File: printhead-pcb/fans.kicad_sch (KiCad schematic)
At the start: 18 parts, among them J4 FAN0, J5 FAN2, J6 FAN1, J7 FAN3, Q1 DTC143E, Q2 DTC143E, Q3 DTC143E, Q4 DTC143E, U2 EMC2302-2-AIZL-TR, U3 EMC2302-2-AIZL-TR

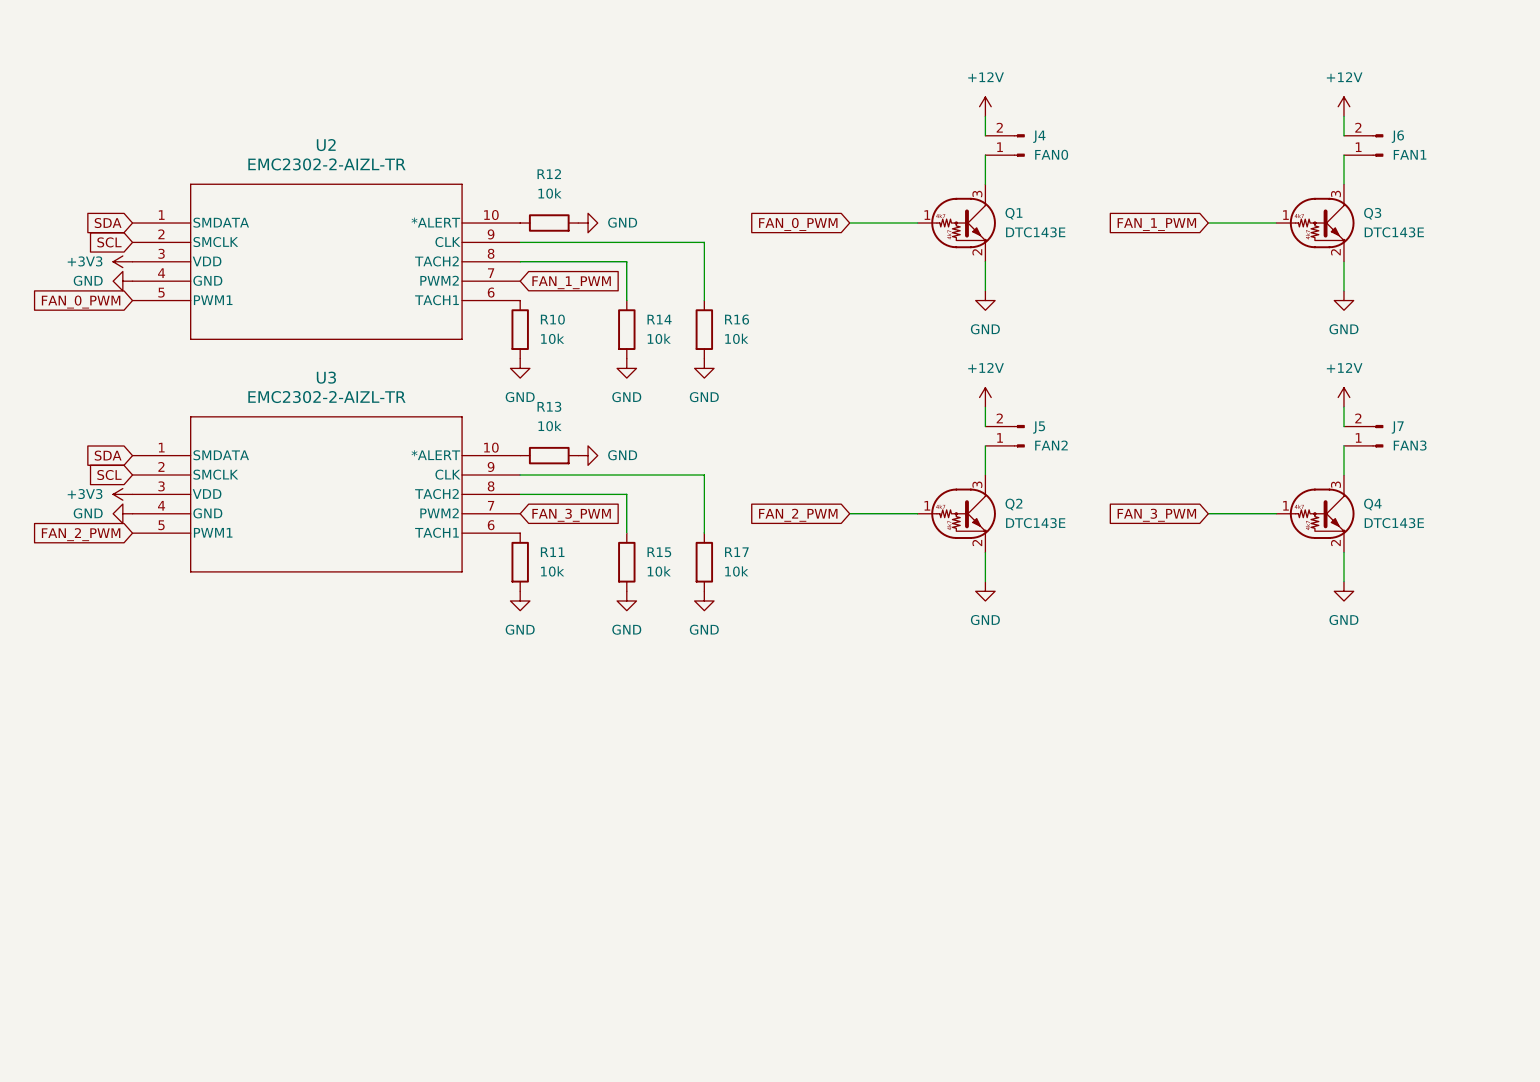
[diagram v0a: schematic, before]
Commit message: removed fan controller and added 2 fans for on off functionality.
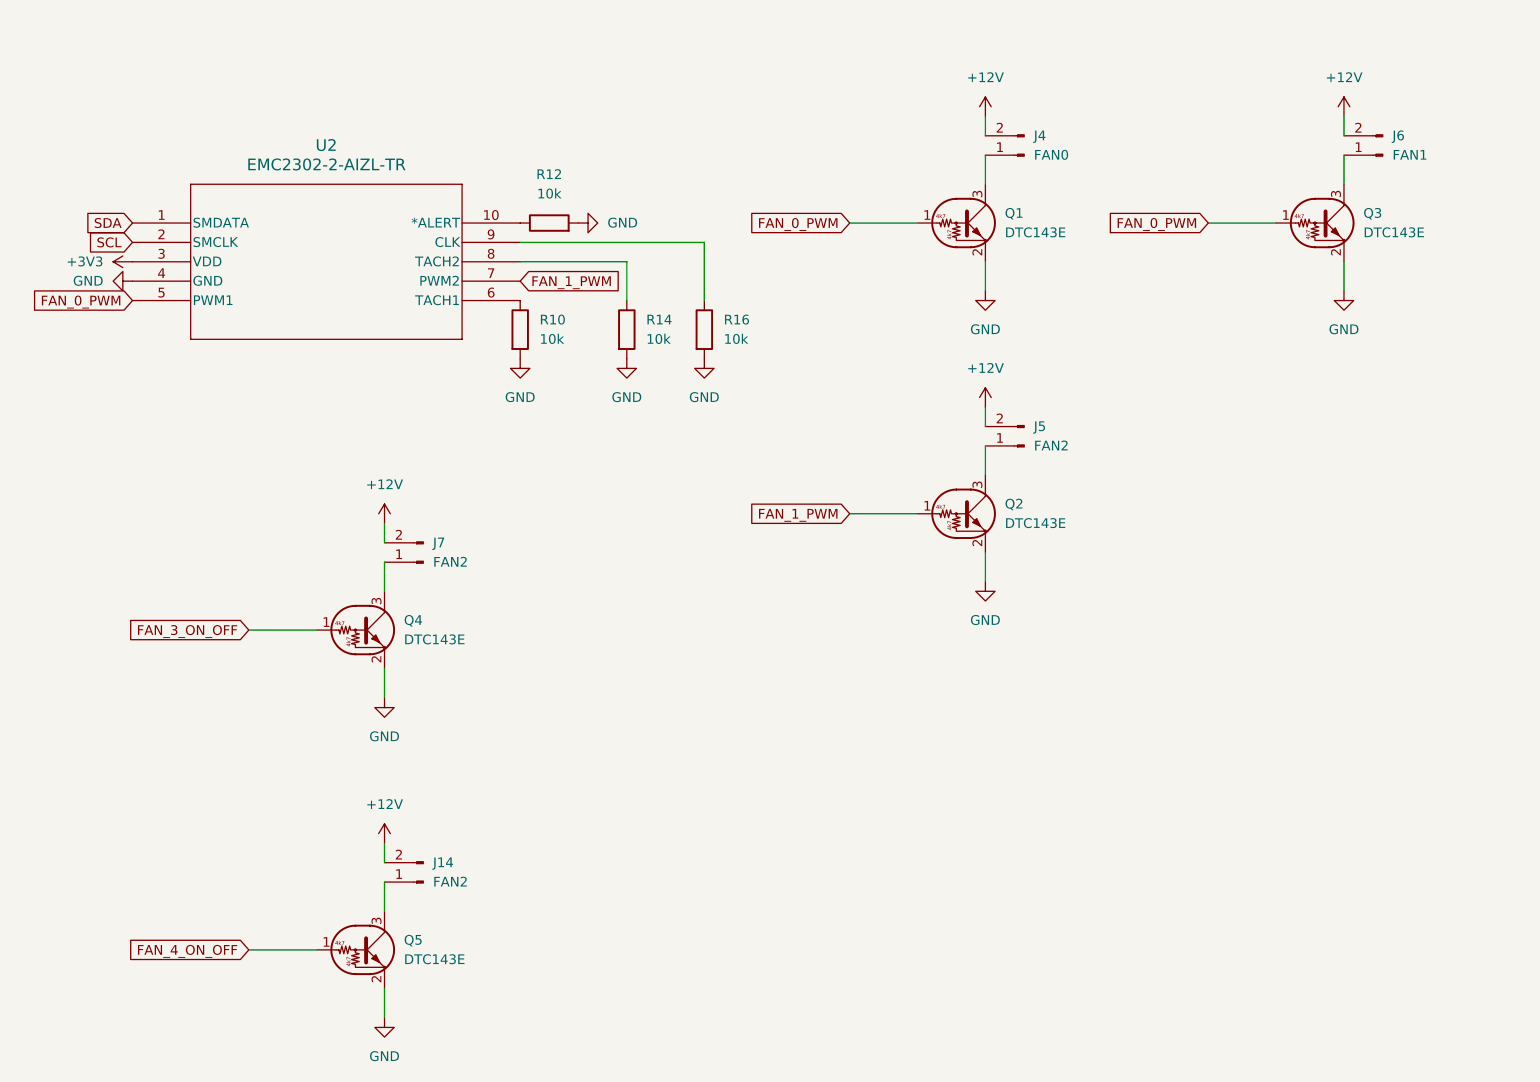
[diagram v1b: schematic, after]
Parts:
- removed R11, R13, R15, R17: 10k, Resistor_SMD:R_0402_1005Metric, symbol Device:R
- removed U3: EMC2302-2-AIZL-TR, EMC2302-2-AIZL-TR:MSOP10_MC_MCH, symbol EMC2302-2-AIZL-TR:EMC2302-2-AIZL-TR
- added J14: FAN2, Connector_JST:JST_EH_B2B-EH-A_1x02_P2.50mm_Vertical, symbol Connector:Conn_01x02_Male
- added Q5: DTC143E, Package_TO_SOT_SMD:SOT-723, symbol Transistor_BJT:DTC143E
- J7: value FAN3 -> FAN2
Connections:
- net FAN_2_PWM is gone; now on net FAN_1_PWM: Q2.1 (B)
- net +12V: now also J14.2 (Pin_2)
- net FAN_0_PWM: now also Q3.1 (B)
- net FAN_1_PWM: no longer Q3.1 (B)
- net GND: now also Q5.2 (E)
- net FAN_3_PWM renamed FAN_3_ON_OFF
- new net: J14.1 (Pin_1), Q5.3 (C)
- new net FAN_4_ON_OFF: Q5.1 (B)

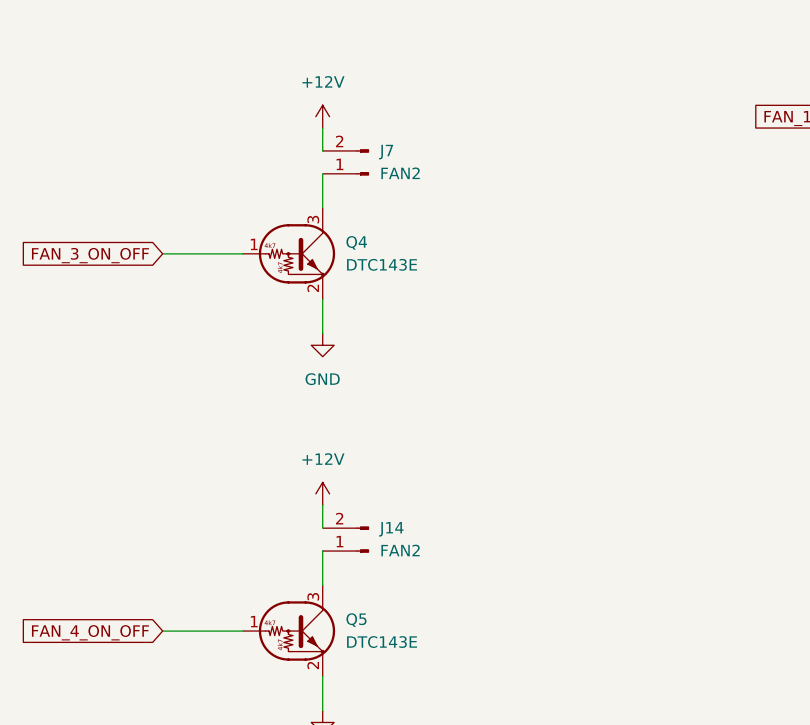
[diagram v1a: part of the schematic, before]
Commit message: changed fan labels
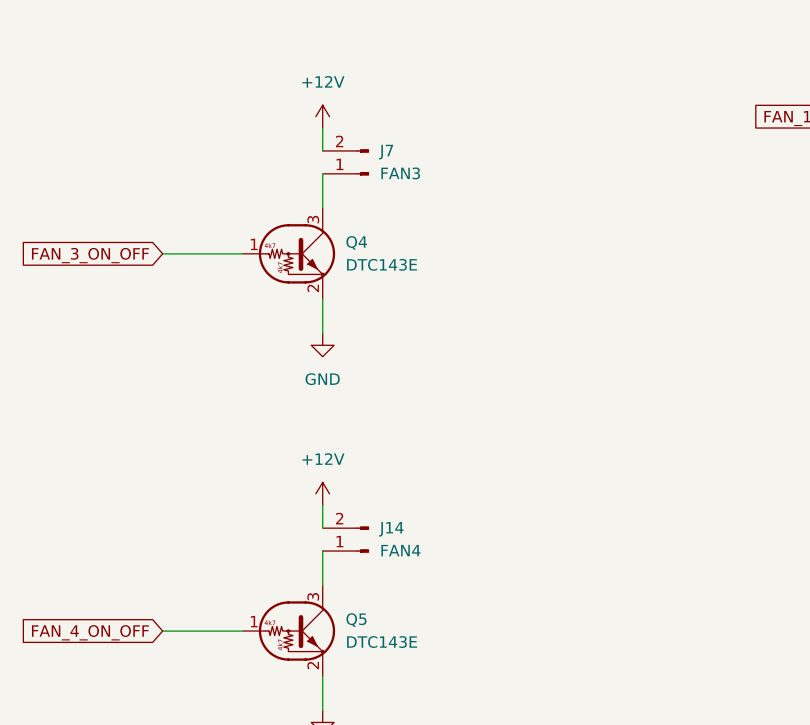
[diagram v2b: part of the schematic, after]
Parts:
- J14: value FAN2 -> FAN4
- J7: value FAN2 -> FAN3
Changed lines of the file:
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@@
 			)
 		)
-		(property "Value" "FAN2"
+		(property "Value" "FAN3"
 			(at 107.95 121.9199 0)
 			(effects
@@
 			)
 		)
-		(property "Value" "FAN2"
+		(property "Value" "FAN4"
 			(at 107.95 163.8299 0)
 			(effects

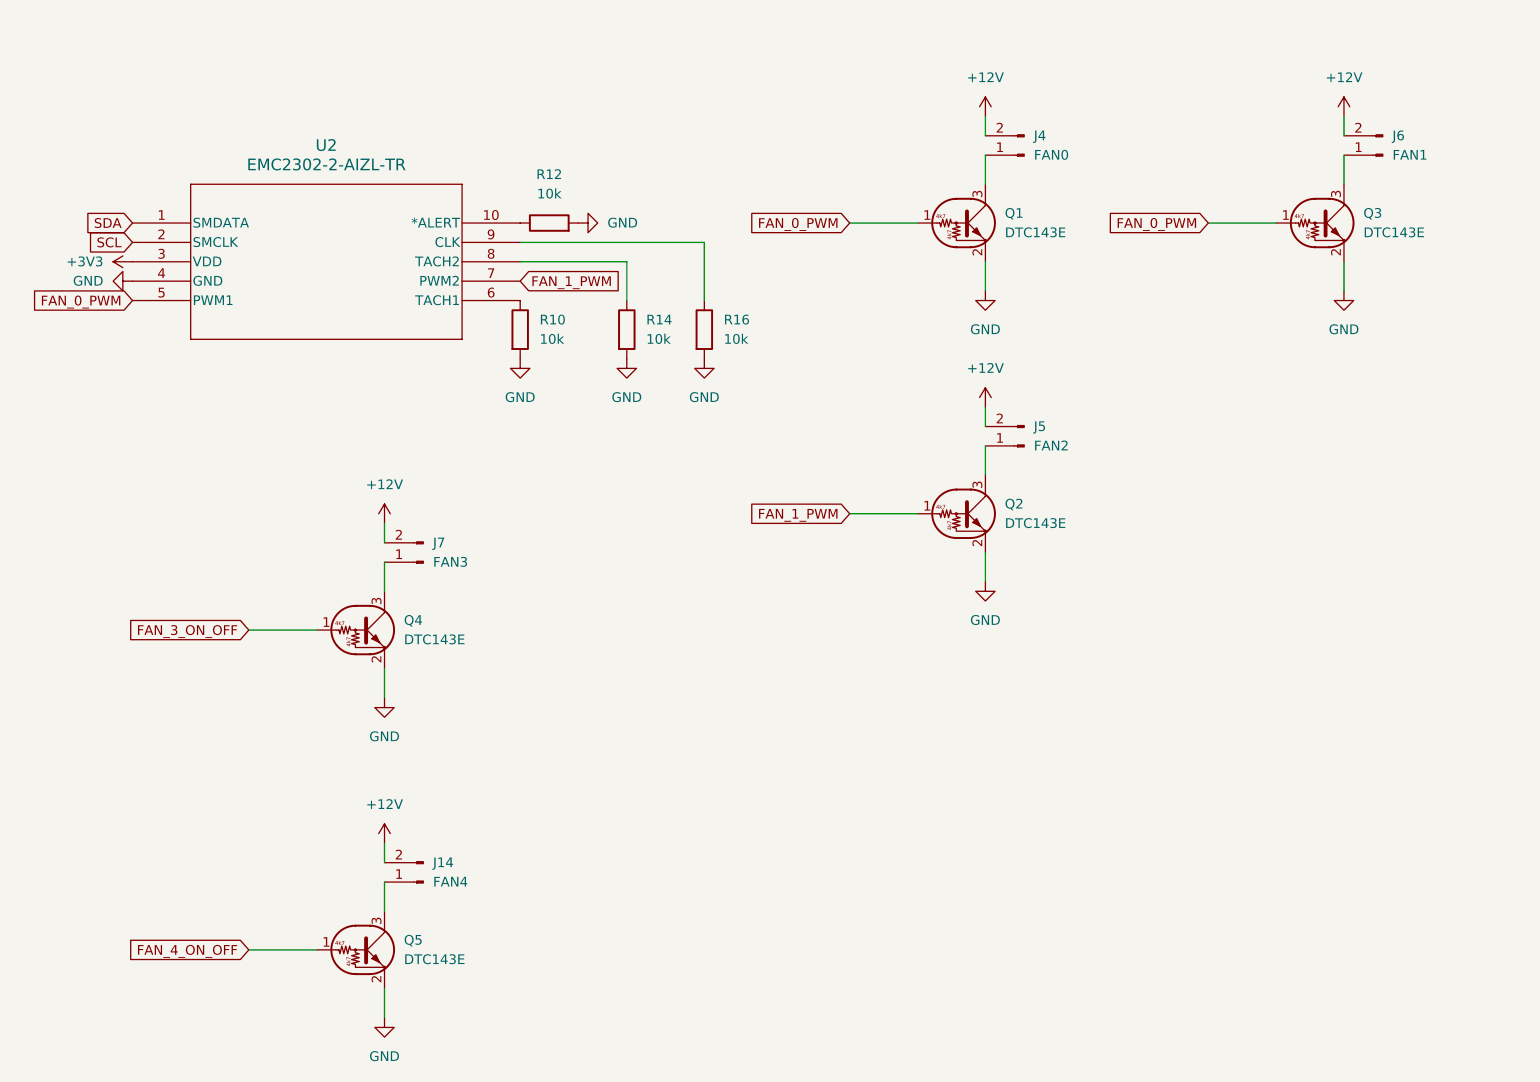
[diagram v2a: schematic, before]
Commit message: removed led driver, added RJ45 (data connector), fan 3. 4. on off
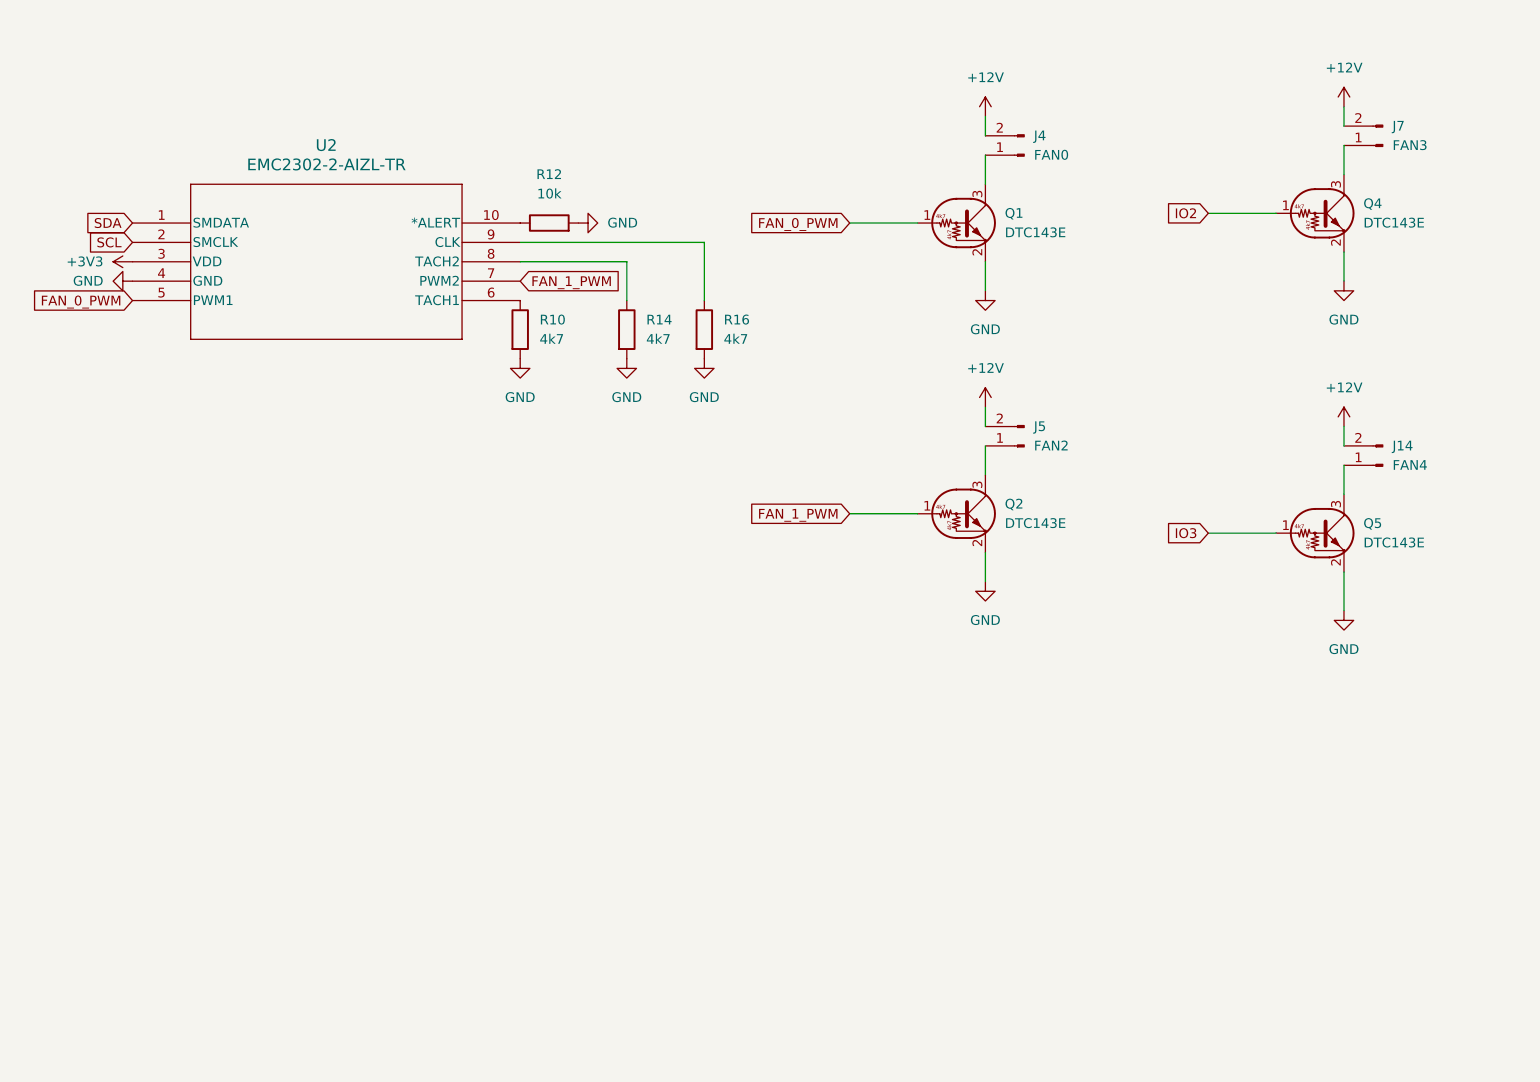
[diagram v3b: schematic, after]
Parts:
- removed J6: FAN1, Connector_JST:JST_EH_S2B-EH_1x02_P2.50mm_Horizontal, symbol Connector:Conn_01x02_Male
- removed Q3: DTC143E, Package_TO_SOT_SMD:SOT-723, symbol Transistor_BJT:DTC143E
- R10, R14, R16: value 10k -> 4k7
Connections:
- net FAN_3_ON_OFF renamed IO2
- net FAN_4_ON_OFF renamed IO3
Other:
- moved on the sheet: J14, J7, Q4, Q5

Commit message: Beschriftungen im Schaltplan hinzugefügt
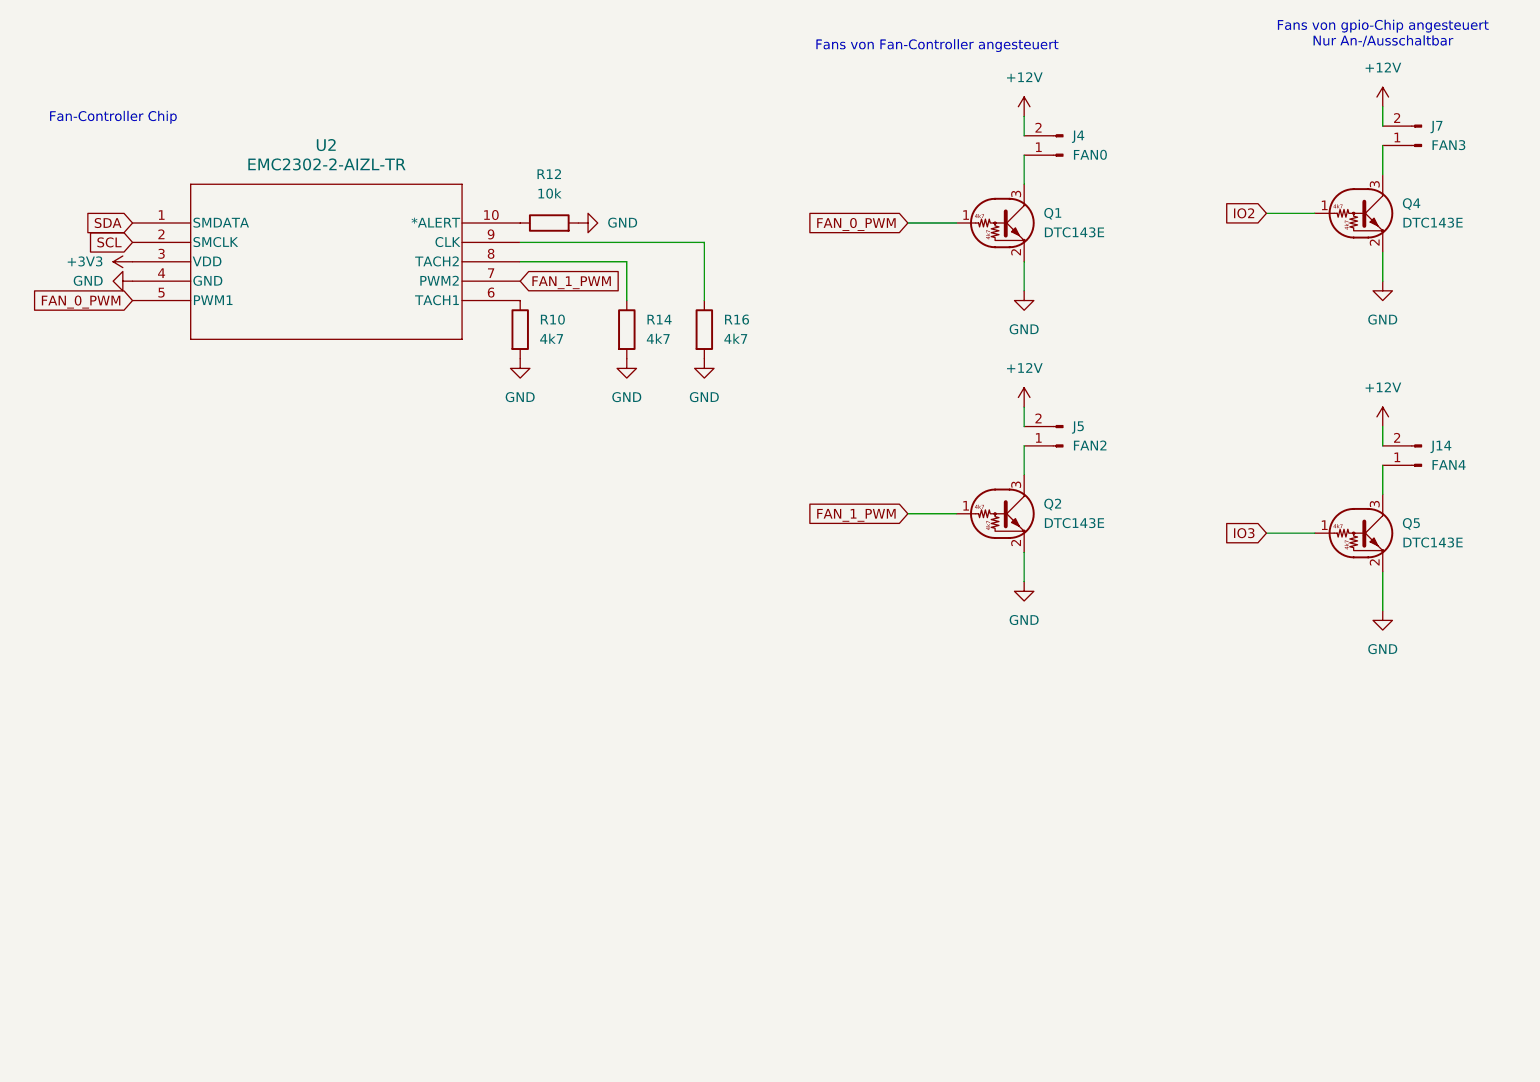
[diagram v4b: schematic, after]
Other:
- note added: "Fan-Controller Chip"
- note added: "Fans von Fan-Controller angesteuert"
- note added: "Fans von gpio-Chip angesteuert Nur An-/Ausschaltbar"
- moved on the sheet: J14, J4, J5, J7, Q1, Q2, Q4, Q5
